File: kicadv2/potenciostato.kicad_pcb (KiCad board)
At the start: 2 copper layers, 100 x 100 mm, 56 parts, among them J1 USB_B_Micro, J10 test_GND, J11 test_GND, J12 test_GND, J13 AC2, J2 test_DAC, J3 Conn_01x03_Male, J4 test_I, J5 test_V, J6 test_DAC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

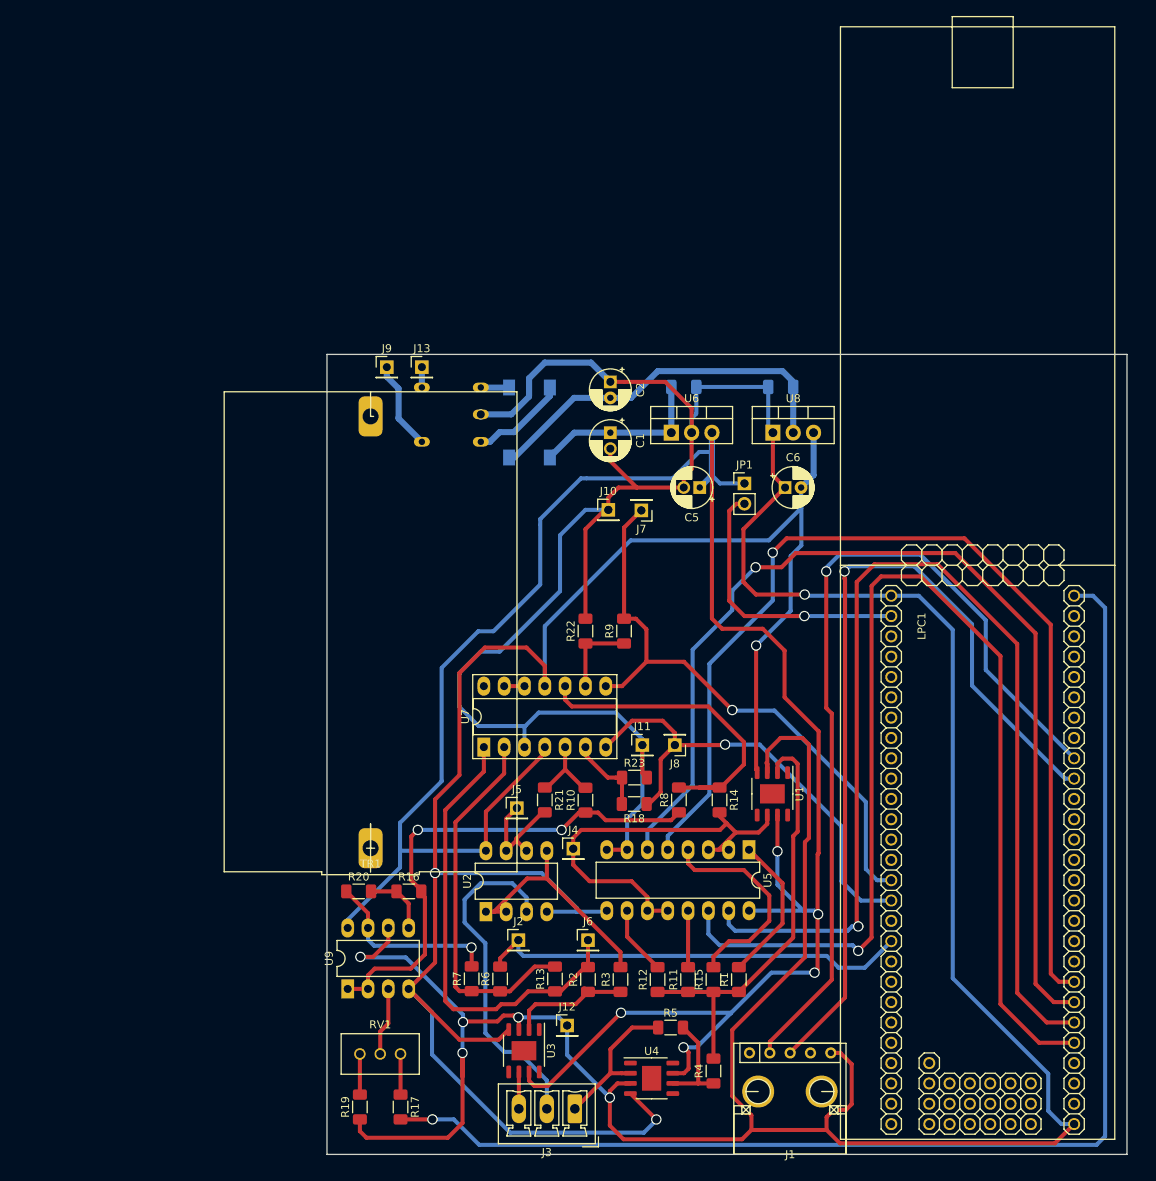
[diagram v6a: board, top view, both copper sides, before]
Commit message: modificaciones esteticas en el pcb y test_DAC por test_VIN
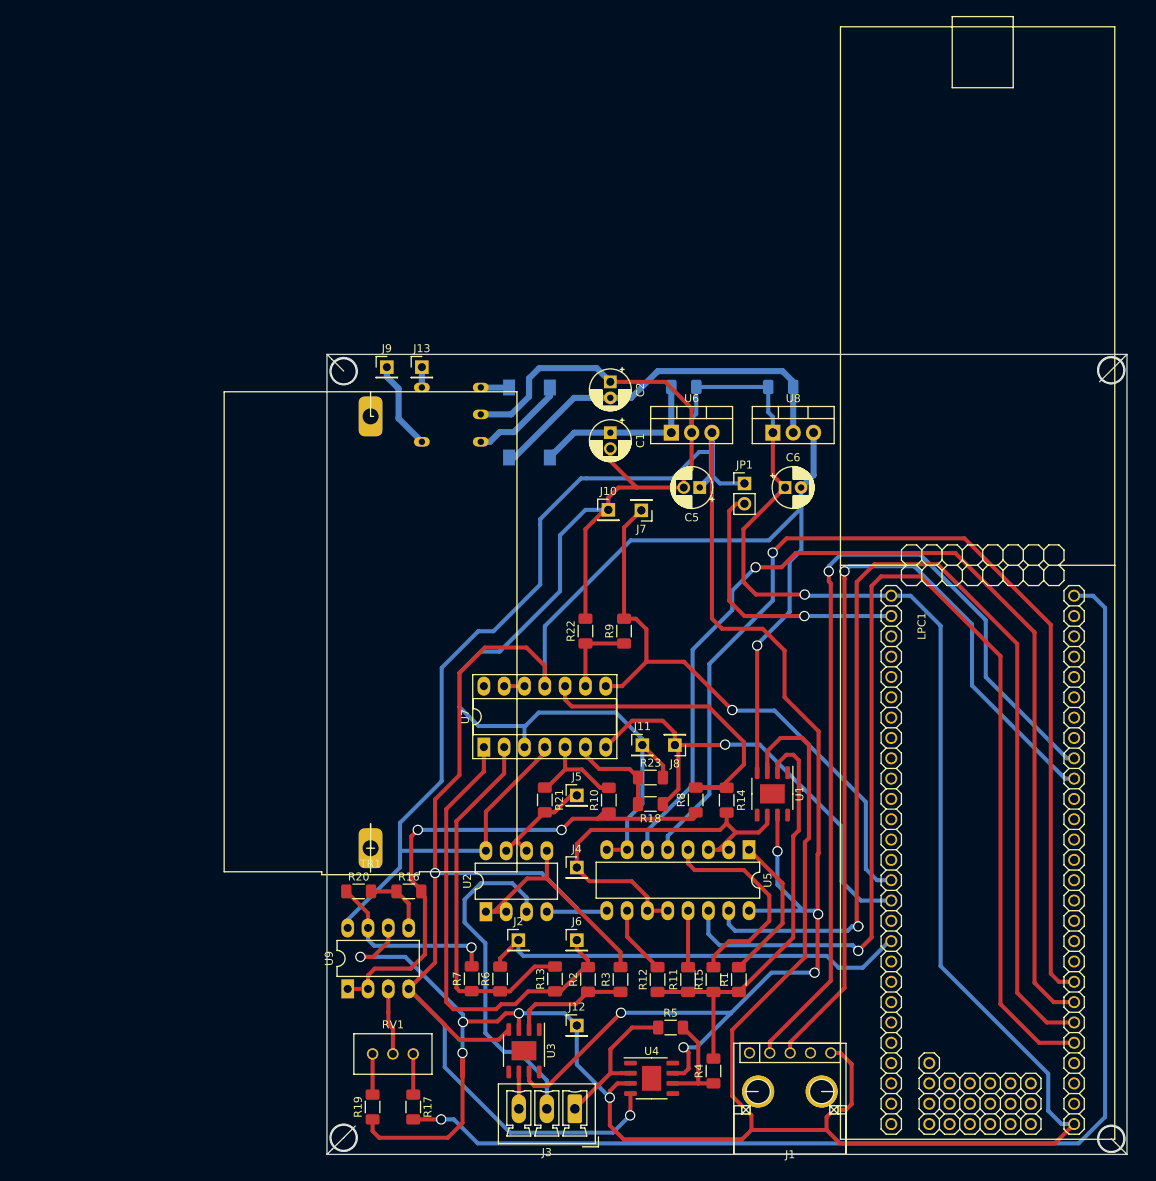
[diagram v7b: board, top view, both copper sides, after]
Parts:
- J6: value test_DAC -> test_VIN
- moved J5 7.66 mm to (149.3, 112.0)
- moved R10 2.92 mm to (153.3, 112.5)
- moved J4 2.39 mm to (149.3, 121.0)
- moved R8 2.10 mm to (164.1, 112.5)
- moved R18 2.03 mm to (158.5, 113.0)
- moved R23 2.01 mm to (158.5, 109.7)
- moved R17 1.59 mm to (128.8, 150.9)
- moved R19 1.59 mm to (123.8, 150.9)
- moved RV1 1.59 mm to (128.8, 144.3)
- moved J6 1.40 mm to (149.3, 130.0)
- moved J12 1.21 mm to (149.3, 140.7)
- moved R14 0.89 mm to (168.0, 112.5)
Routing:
- net -5V: track 240.9 -> 235.8 mm
- net /salida_dac/VOffset: track 63.4 -> 67.5 mm
- net Net-(R10-Pad2): track 9.50 -> 12.7 mm
- net /salida_dac/3V3: track 160.4 -> 157.2 mm
- net Net-(R14-Pad1): track 40.9 -> 38.3 mm
- net Net-(R18-Pad2): track 10.1 -> 12.1 mm
- net /salida_dac/I_IN: track 52.9 -> 51.4 mm
- net /salida_dac/V_IN: track 14.3 -> 13.3 mm
- net Net-(R1-Pad1): track 54.9 -> 55.7 mm
- net Net-(J1-Pad2): track 109.6 -> 110.1 mm, vias 2 -> 3
- net Net-(J1-Pad3): track 107.5 -> 107.4 mm, vias 2 -> 3
- net Net-(LPC1-Pad9): vias 0 -> 1
- net Net-(LPC1-Pad8): vias 0 -> 1
- net Net-(LPC1-Pad7): vias 0 -> 1
- net Net-(LPC1-Pad6): vias 0 -> 1
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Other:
- outline, holes or cut-outs redrawn

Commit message: planos de masa, gerber
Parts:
- moved C6 3.21 mm to (178.5, 73.5), turned to 180 degrees
- moved R17 2.09 mm to (128.3, 148.9)
- moved RV1 2.09 mm to (128.3, 142.2)
- moved R19 2.09 mm to (123.3, 148.9)
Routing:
- net GND: track 526.3 -> 0.00 mm, vias 22 -> 6
- net -5V: track 235.8 -> 229.7 mm, vias 8 -> 3
- net /salida_dac/VOffset: track 67.5 -> 64.7 mm, vias 4 -> 2
- net Net-(RV1-Pad2): track 8.36 -> 6.12 mm, vias 2 -> 0
- net /salida_dac/3V3: track 157.2 -> 158.7 mm, vias 2 -> 1
- net /salida_dac/gan_x0.1: track 139.6 -> 138.6 mm, vias 3 -> 1
- net /salida_dac/gan_x10: track 144.3 -> 143.5 mm, vias 3 -> 1
- net Net-(J1-Pad2): track 110.1 -> 109.4 mm, vias 3 -> 1
- net /salida_dac/I_IN: track 51.4 -> 51.2 mm, vias 5 -> 0
- net /salida_dac/-VOffset: track 22.9 -> 22.7 mm, vias 2 -> 1
- net Net-(J7-Pad1): track 75.0 -> 74.8 mm, vias 4 -> 1
- net +5V: track 283.0 -> 282.8 mm, vias 11 -> 5
- net Net-(R19-Pad2): vias 1 -> 0
- net Net-(R17-Pad1): vias 1 -> 0
- net Net-(U7-Pad14): vias 1 -> 0
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- added copper zone on B.Cu, net GND
- added copper zone on F.Cu, net GND
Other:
- outline, holes or cut-outs redrawn
